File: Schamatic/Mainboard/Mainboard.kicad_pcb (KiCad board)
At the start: 2 copper layers, 85 parts, among them J1 BAT+, J10 BAT-, J2 M+1, J3 USART, J4 3.3V, J5 CONN_02X04, J6 FTSH-105-01-F-D-K, J7 M+2, J8 M-1, J9 M-2, Q1 BSC030P03NS3GAUMA1, SW1 B3U-1000P, SW2 B3U-1000P, SW3 B3U-1000P, SW4 B3U-1000P, U1 ACS781, U2 ADP2303ARDZ-3.3, U3 cc3220, U4 DEA202450BT, U5 MX25R3235F, U6 LSM9DS1, Y1 32.768kHz, Y2 40Mhz

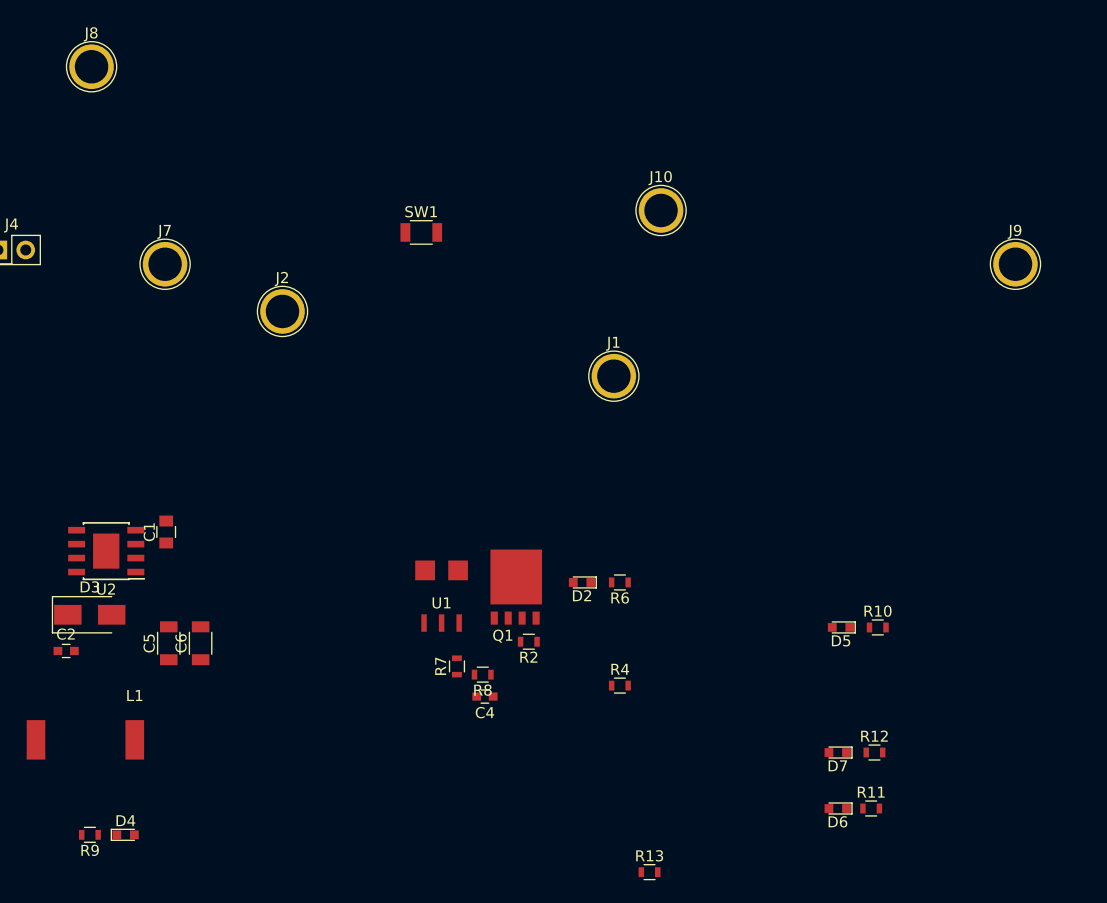
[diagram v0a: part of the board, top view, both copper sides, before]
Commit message: pushbutton switch
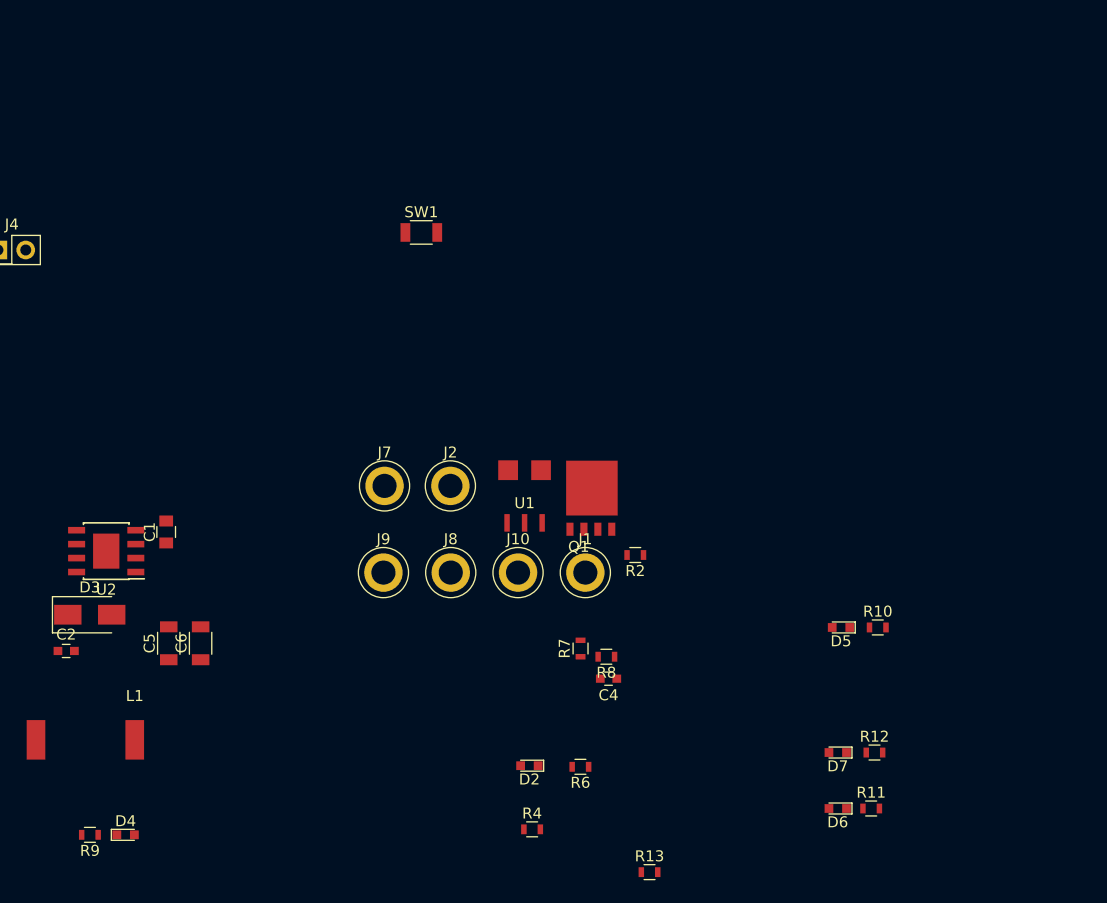
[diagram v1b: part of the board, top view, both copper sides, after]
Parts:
- moved J9 64.1 mm to (118.9, 50.4)
- moved J8 56.5 mm to (125.0, 50.4)
- moved J10 35.5 mm to (131.2, 50.4)
- moved J7 28.4 mm to (119.0, 42.5)
- moved J2 22.1 mm to (125.0, 42.5)
- moved J1 18.1 mm to (137.3, 50.4)
- moved D2 17.4 mm to (132.2, 68.0)
- moved R6 17.2 mm to (136.8, 68.1)
- moved R4 15.3 mm to (132.4, 73.8)
- moved R2 12.5 mm to (141.8, 48.8)
- moved U1 11.9 mm to (131.8, 43.5)
- moved R7 11.4 mm to (136.9, 57.3)
- moved R8 11.4 mm to (139.2, 58.1)
- moved C4 11.4 mm to (139.4, 60.1)
- moved Q1 10.6 mm to (135.9, 46.5)
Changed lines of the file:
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@@
     (mod_text_size 1 1)
     (mod_text_width 0.15)
-    (pad_size 1.524 1.524)
-    (pad_drill 0.762)
+    (pad_size 3.5 3.5)
+    (pad_drill 2.2)
     (pad_to_mask_clearance 0.2)
     (aux_axis_origin 0 0)
@@
   )
   (module Capacitors_SMD:C_0603 (layer F.Cu)
-    (at 128.15 61.7 180)
+    (at 139.41357 60.069586 180)
     (descr "Capacitor SMD 0603, reflow soldering, AVX (see smccp.pdf)")
     (tags "capacitor 0603")
@@
   )
   (module Dizzy:BSC030P (layer F.Cu)
-    (at 129 54.55)
+    (at 135.9 46.45)
     (fp_text reference Q1 (at 0.8 1.6) (layer F.SilkS)
       (effects (font (size 1 1) (thickness 0.15)))
@@
   )
   (module Resistors_SMD:R_0603 (layer F.Cu)
-    (at 132.15 56.7 180)
+    (at 141.85 48.8 180)
     (descr "Resistor SMD 0603, reflow soldering, Vishay (see dcrcw.pdf)")
     (tags "resistor 0603")
@@
   )
   (module Resistors_SMD:R_0603 (layer F.Cu)
-    (at 140.45 60.7)
+    (at 132.45 73.8)
     (descr "Resistor SMD 0603, reflow soldering, Vishay (see dcrcw.pdf)")
     (tags "resistor 0603")
@@
   )
   (module Resistors_SMD:R_0603 (layer F.Cu)
-    (at 140.45 51.3 180)
+    (at 136.85 68.1 180)
     (descr "Resistor SMD 0603, reflow soldering, Vishay (see dcrcw.pdf)")
     (tags "resistor 0603")
@@
   )
   (module Resistors_SMD:R_0603 (layer F.Cu)
-    (at 125.6 58.95 90)
+    (at 136.86357 57.319586 90)
     (descr "Resistor SMD 0603, reflow soldering, Vishay (see dcrcw.pdf)")
     (tags "resistor 0603")
@@
   )
   (module Resistors_SMD:R_0603 (layer F.Cu)
-    (at 127.95 59.7 180)
+    (at 139.21357 58.069586 180)
     (descr "Resistor SMD 0603, reflow soldering, Vishay (see dcrcw.pdf)")
     (tags "resistor 0603")
@@
   )
   (module Dizzy:ACS781 (layer F.Cu)
-    (at 124.2 52.6)
+    (at 131.76357 43.469586)
     (fp_text reference U1 (at 0 0.6) (layer F.SilkS)
       (effects (font (size 1 1) (thickness 0.15)))
@@
   )
   (module LEDs:LED_0603 (layer F.Cu)
-    (at 137 51.3 180)
+    (at 132.2 68 180)
     (descr "LED 0603 smd package")
     (tags "LED led 0603 SMD smd SMT smt smdled SMDLED smtled SMTLED")
@@
   )
   (module Connectors:1pin (layer F.Cu)
-    (at 139.9 32.5)
+    (at 137.299999 50.4)
     (descr "module 1 pin (ou trou mecanique de percage)")
     (tags DEV)
@@
     (fp_circle (center 0 0) (end 2.6 0) (layer F.CrtYd) (width 0.05))
     (fp_circle (center 0 0) (end 0 -2.286) (layer F.SilkS) (width 0.12))
-    (pad 1 thru_hole circle (at 0 0) (size 4.064 4.064) (drill 3.048) (layers *.Cu *.Mask)
+    (pad 1 thru_hole circle (at 0 0) (size 3.5 3.5) (drill 2.2) (layers *.Cu *.Mask)
       (net 79 "Net-(J1-Pad1)"))
   )
   (module Connectors:1pin (layer F.Cu)
-    (at 109.7 26.6)
+    (at 125 42.5)
     (descr "module 1 pin (ou trou mecanique de percage)")
     (tags DEV)
@@
     (fp_circle (center 0 0) (end 2.6 0) (layer F.CrtYd) (width 0.05))
     (fp_circle (center 0 0) (end 0 -2.286) (layer F.SilkS) (width 0.12))
-    (pad 1 thru_hole circle (at 0 0) (size 4.064 4.064) (drill 3.048) (layers *.Cu *.Mask)
+    (pad 1 thru_hole circle (at 0 0) (size 3.5 3.5) (drill 2.2) (layers *.Cu *.Mask)
       (net 78 "Net-(J2-Pad1)"))
   )
@@
   )
   (module Connectors:1pin (layer F.Cu)
-    (at 99 22.3)
+    (at 119 42.5)
     (descr "module 1 pin (ou trou mecanique de percage)")
     (tags DEV)
@@
     (fp_circle (center 0 0) (end 2.6 0) (layer F.CrtYd) (width 0.05))
     (fp_circle (center 0 0) (end 0 -2.286) (layer F.SilkS) (width 0.12))
-    (pad 1 thru_hole circle (at 0 0) (size 4.064 4.064) (drill 3.048) (layers *.Cu *.Mask)
+    (pad 1 thru_hole circle (at 0 0) (size 3.5 3.5) (drill 2.2) (layers *.Cu *.Mask)
       (net 78 "Net-(J2-Pad1)"))
   )
   (module Connectors:1pin (layer F.Cu)
-    (at 92.3 4.3)
+    (at 125.033333 50.4)
     (descr "module 1 pin (ou trou mecanique de percage)")
     (tags DEV)
@@
     (fp_circle (center 0 0) (end 2.6 0) (layer F.CrtYd) (width 0.05))
     (fp_circle (center 0 0) (end 0 -2.286) (layer F.SilkS) (width 0.12))
-    (pad 1 thru_hole circle (at 0 0) (size 4.064 4.064) (drill 3.048) (layers *.Cu *.Mask)
+    (pad 1 thru_hole circle (at 0 0) (size 3.5 3.5) (drill 2.2) (layers *.Cu *.Mask)
       (net 1 Earth))
   )
   (module Connectors:1pin (layer F.Cu)
-    (at 176.5 22.3)
+    (at 118.9 50.4)
     (descr "module 1 pin (ou trou mecanique de percage)")
     (tags DEV)
@@
     (fp_circle (center 0 0) (end 2.6 0) (layer F.CrtYd) (width 0.05))
     (fp_circle (center 0 0) (end 0 -2.286) (layer F.SilkS) (width 0.12))
-    (pad 1 thru_hole circle (at 0 0) (size 4.064 4.064) (drill 3.048) (layers *.Cu *.Mask)
+    (pad 1 thru_hole circle (at 0 0) (size 3.5 3.5) (drill 2.2) (layers *.Cu *.Mask)
       (net 1 Earth))
   )
   (module Connectors:1pin (layer F.Cu)
-    (at 144.2 17.4)
+    (at 131.166666 50.4)
     (descr "module 1 pin (ou trou mecanique de percage)")
     (tags DEV)
@@
     (fp_circle (center 0 0) (end 2.6 0) (layer F.CrtYd) (width 0.05))
     (fp_circle (center 0 0) (end 0 -2.286) (layer F.SilkS) (width 0.12))
-    (pad 1 thru_hole circle (at 0 0) (size 4.064 4.064) (drill 3.048) (layers *.Cu *.Mask)
-      (net 1 Earth))
-  )
+    (pad 1 thru_hole circle (at 0 0) (size 3.5 3.5) (drill 2.2) (layers *.Cu *.Mask)
+      (net 1 Earth))
+  )

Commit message: continue motherboard
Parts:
- added C35: 0.1uF, Capacitors_SMD:C_0603, F.Cu at (134.8, 44.6)
- added C36: 0.1uF, Capacitors_SMD:C_0603, F.Cu at (106.3, 104.8)
- added D1: D, Diodes_SMD:D_SMA, F.Cu at (147.2, 48.7)
- added D8: D, Diodes_SMD:D_SMA, F.Cu at (153.7, 48.7)
- added J11: PLUG+, Connectors:1pin, F.Cu at (147.0, 42.0)
- added J12: PLUG-, Connectors:1pin, F.Cu at (153.3, 56.5)
- added R17: 100k, Resistors_SMD:R_0603, F.Cu at (139.8, 46.7)
- added R18: 1.4M, Resistors_SMD:R_0603, F.Cu at (142.5, 42.4)
- added R19: 100k, Resistors_SMD:R_0603, F.Cu at (142.5, 45.1)
- added U7: LTC2954, Housings_DFN_QFN:DFN-8-1EP_2x3mm_Pitch0.5mm, F.Cu at (139.6, 42.8)
- added U8: LTC2876, Dizzy:LTC2876, F.Cu at (110.4, 104.7)
- R2: value R -> 100k
- moved SW4 111.6 mm to (108.0, 131.7), turned to 180 degrees
- moved R3 97.3 mm to (111.7, 41.8), turned to 90 degrees
- moved SW3 93.5 mm to (95.2, 97.9)
- moved D5 92.8 mm to (93.7, 119.7)
- moved R10 92.7 mm to (97.0, 119.5)
- moved J3 87.7 mm to (104.3, 98.8), turned to 270 degrees
- moved SW2 84.8 mm to (95.2, 102.4)
- moved C30 84.2 mm to (103.3, 120.1)
- moved D7 79.5 mm to (93.7, 110.3)
- moved R12 79.5 mm to (97.0, 110.3)
- moved D6 79.3 mm to (93.7, 115.0)
- moved R11 79.3 mm to (96.8, 115.0)
- moved R1 78.1 mm to (104.2, 122.5)
- moved J6 74.0 mm to (107.4, 121.3)
- moved R13 54.5 mm to (111.8, 122.3)
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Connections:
- J1 pad 1: Net-(J1-Pad1) -> Net-(D8-Pad2)
- J3 pad 1: RX -> RS-B
- J3 pad 2: TX -> RS-A
- Q1 pad 3: Net-(J1-Pad1) -> Net-(C35-Pad2)
- R2 pad 1: Net-(Q1-Pad2) -> Net-(R17-Pad1)
- R2 pad 2: Net-(J1-Pad1) -> Net-(C35-Pad2)
- SW1 pad 1: Net-(Q1-Pad2) -> Earth
- SW1 pad 2: Earth -> Net-(SW1-Pad2)
- U3 pad 3: Net-(U3-Pad3) -> DE

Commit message: working on mainboard PCB
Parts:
- added J13: MOUNT, Mounting_Holes:MountingHole_3.5mm_Pad, F.Cu at (145.8, 128.7)
- added J14: MOUNT, Mounting_Holes:MountingHole_3.5mm_Pad, F.Cu at (88.8, 128.8)
- added J15: MOUNT, Mounting_Holes:MountingHole_3.5mm_Pad, F.Cu at (146.0, 80.0)
- added J16: MOUNT, Mounting_Holes:MountingHole_3.5mm_Pad, F.Cu at (88.5, 80.0)
- added SW5: B3U-1000P, Resistors_SMD:R_1206, F.Cu at (88.8, 103.3)
- AE1: value AH316M245001-T -> ANT
- Q1: value BSC030P03NS3GAUMA1 -> p-MOSFET
- moved R15 83.2 mm to (97.8, 124.1), turned to 270 degrees
- moved R14 77.9 mm to (101.8, 130.9), turned to 180 degrees
- moved J1 61.3 mm to (139.5, 101.7), turned to 270 degrees
- moved J11 59.6 mm to (146.0, 101.6), turned to 270 degrees
- moved J4 51.2 mm to (89.0, 94.8), turned to 270 degrees
- moved D8 48.2 mm to (139.5, 94.8), turned to 270 degrees
- moved R16 47.2 mm to (100.4, 113.5), turned to 270 degrees
- moved D1 46.2 mm to (146.0, 94.9), turned to 270 degrees
- moved J2 41.8 mm to (116.5, 87.3)
- moved J7 41.8 mm to (110.5, 87.3)
- moved D3 41.8 mm to (88.9, 87.7), turned to 90 degrees
- moved R6 39.9 mm to (122.7, 81.1)
- moved Q1 38.6 mm to (133.4, 90.9)
- moved R17 38.6 mm to (131.8, 84.4)
- moved U1 38.6 mm to (123.3, 88.1)
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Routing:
- net 3v3: track 0.00 -> 186.8 mm, vias 0 -> 18
- net VDD_ANA: track 0.00 -> 50.6 mm
- net 12V: track 0.00 -> 47.1 mm
- net VDD_DIG: track 0.00 -> 42.9 mm
- net Net-(D5-Pad2): track 0.00 -> 40.1 mm, vias 0 -> 2
- net Net-(SW5-Pad2): track 0.00 -> 37.9 mm, vias 0 -> 2
- net Net-(C35-Pad2): track 0.00 -> 34.9 mm, vias 0 -> 2
- net SCL: track 0.00 -> 34.0 mm, vias 0 -> 3
- net Net-(SW3-Pad2): track 0.00 -> 32.1 mm, vias 0 -> 2
- net Net-(D6-Pad2): track 0.00 -> 31.9 mm, vias 0 -> 2
- net SDA: track 0.00 -> 31.0 mm, vias 0 -> 2
- net nRESET: track 0.00 -> 30.2 mm, vias 0 -> 2
- net Earth: track 0.00 -> 29.7 mm, vias 0 -> 59
- net Net-(SW2-Pad2): track 0.00 -> 29.0 mm, vias 0 -> 2
- net Net-(D7-Pad2): track 0.00 -> 25.2 mm, vias 0 -> 2
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- added copper zone on F.Cu, net 12V
- added copper zone on In2.Cu, net 3v3
- added copper zone on B.Cu, net Earth
- added copper zone on F.Cu, net Earth
- added copper zone on In1.Cu, net Earth
- added copper zone on F.Cu, net Net-(C35-Pad2)
- added copper zone on F.Cu, net Net-(D1-Pad2)
- added copper zone on F.Cu, net Net-(D8-Pad2)
- added copper zone on F.Cu, net Net-(J2-Pad1)
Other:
- board outline added: 70 x 74.3 mm
- copper layers 2 -> 4
- net class Default: clearance 0.2 -> 0.13; trace_width 0.25 -> 0.13; via_dia 0.6 -> 0.4; via_drill 0.4 -> 0.25
- rule trace_clearance: 0.2 -> 0.13
- rule trace_min: 0.2 -> 0.1
- rule via_min_drill: 0.3 -> 0.2
- rule via_min_size: 0.4 -> 0.2
- board text added: "DizzyRobot"

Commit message: mainboard pcb more or less complete
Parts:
- added REF**: VIA-0.4, Dizzy:VIA-0.4, F.Cu at (105.8, 104.6)
- added REF**: VIA-0.4, Dizzy:VIA-0.4, F.Cu at (101.0, 117.6)
- added REF**: VIA-0.4, Dizzy:VIA-0.4, F.Cu at (125.4, 114.0)
- added REF**: VIA-0.4, Dizzy:VIA-0.4, F.Cu at (125.4, 114.8)
- added REF**: VIA-0.4, Dizzy:VIA-0.4, F.Cu at (125.4, 113.2)
- added REF**: VIA-0.4, Dizzy:VIA-0.4, F.Cu at (125.4, 107.6)
- added REF**: VIA-0.4, Dizzy:VIA-0.4, F.Cu at (125.4, 110.0)
- added REF**: VIA-0.4, Dizzy:VIA-0.4, F.Cu at (125.4, 108.4)
- added REF**: VIA-0.4, Dizzy:VIA-0.4, F.Cu at (125.4, 110.8)
- added REF**: VIA-0.4, Dizzy:VIA-0.4, F.Cu at (125.4, 109.2)
- added REF**: VIA-0.4, Dizzy:VIA-0.4, F.Cu at (124.6, 111.6)
- added REF**: VIA-0.4, Dizzy:VIA-0.4, F.Cu at (124.6, 112.4)
- added REF**: VIA-0.4, Dizzy:VIA-0.4, F.Cu at (92.3, 116.8)
- added REF**: VIA-0.4, Dizzy:VIA-0.4, F.Cu at (124.6, 114.0)
- added REF**: VIA-0.4, Dizzy:VIA-0.4, F.Cu at (124.6, 114.8)
- added REF**: VIA-0.4, Dizzy:VIA-0.4, F.Cu at (124.6, 113.2)
- added REF**: VIA-0.4, Dizzy:VIA-0.4, F.Cu at (124.6, 107.6)
- added REF**: VIA-0.4, Dizzy:VIA-0.4, F.Cu at (124.6, 110.0)
- added REF**: VIA-0.4, Dizzy:VIA-0.4, F.Cu at (124.6, 108.4)
- added REF**: VIA-0.4, Dizzy:VIA-0.4, F.Cu at (124.6, 110.8)
- added REF**: VIA-0.4, Dizzy:VIA-0.4, F.Cu at (124.6, 109.2)
- added REF**: VIA-0.4, Dizzy:VIA-0.4, F.Cu at (123.8, 111.6)
- added REF**: VIA-0.4, Dizzy:VIA-0.4, F.Cu at (123.8, 112.4)
- added REF**: VIA-0.4, Dizzy:VIA-0.4, F.Cu at (95.5, 123.2)
- added REF**: VIA-0.4, Dizzy:VIA-0.4, F.Cu at (123.8, 114.0)
- added REF**: VIA-0.4, Dizzy:VIA-0.4, F.Cu at (123.8, 114.8)
- added REF**: VIA-0.4, Dizzy:VIA-0.4, F.Cu at (123.8, 113.2)
- added REF**: VIA-0.4, Dizzy:VIA-0.4, F.Cu at (123.8, 107.6)
- added REF**: VIA-0.4, Dizzy:VIA-0.4, F.Cu at (123.8, 110.0)
- added REF**: VIA-0.4, Dizzy:VIA-0.4, F.Cu at (123.8, 108.4)
- added REF**: VIA-0.4, Dizzy:VIA-0.4, F.Cu at (123.8, 110.8)
- added REF**: VIA-0.4, Dizzy:VIA-0.4, F.Cu at (123.8, 109.2)
- added REF**: VIA-0.4, Dizzy:VIA-0.4, F.Cu at (123.0, 111.6)
- added REF**: VIA-0.4, Dizzy:VIA-0.4, F.Cu at (123.0, 112.4)
- added REF**: VIA-0.4, Dizzy:VIA-0.4, F.Cu at (118.8, 129.0)
- added REF**: VIA-0.4, Dizzy:VIA-0.4, F.Cu at (123.0, 114.0)
- added REF**: VIA-0.4, Dizzy:VIA-0.4, F.Cu at (123.0, 114.8)
- added REF**: VIA-0.4, Dizzy:VIA-0.4, F.Cu at (123.0, 113.2)
- added REF**: VIA-0.4, Dizzy:VIA-0.4, F.Cu at (123.0, 107.6)
- added REF**: VIA-0.4, Dizzy:VIA-0.4, F.Cu at (123.0, 110.0)
- added REF**: VIA-0.4, Dizzy:VIA-0.4, F.Cu at (123.0, 108.4)
- added REF**: VIA-0.4, Dizzy:VIA-0.4, F.Cu at (123.0, 110.8)
- added REF**: VIA-0.4, Dizzy:VIA-0.4, F.Cu at (123.0, 109.2)
- added REF**: VIA-0.4, Dizzy:VIA-0.4, F.Cu at (122.2, 111.6)
- added REF**: VIA-0.4, Dizzy:VIA-0.4, F.Cu at (122.2, 112.4)
- added REF**: VIA-0.4, Dizzy:VIA-0.4, F.Cu at (110.7, 129.0)
- added REF**: VIA-0.4, Dizzy:VIA-0.4, F.Cu at (122.2, 114.0)
- added REF**: VIA-0.4, Dizzy:VIA-0.4, F.Cu at (122.2, 114.8)
- added REF**: VIA-0.4, Dizzy:VIA-0.4, F.Cu at (122.2, 113.2)
- added REF**: VIA-0.4, Dizzy:VIA-0.4, F.Cu at (122.2, 107.6)
- added REF**: VIA-0.4, Dizzy:VIA-0.4, F.Cu at (122.2, 110.0)
- added REF**: VIA-0.4, Dizzy:VIA-0.4, F.Cu at (122.2, 108.4)
- added REF**: VIA-0.4, Dizzy:VIA-0.4, F.Cu at (122.2, 110.8)
- added REF**: VIA-0.4, Dizzy:VIA-0.4, F.Cu at (122.2, 109.2)
- added REF**: VIA-0.4, Dizzy:VIA-0.4, F.Cu at (121.4, 111.6)
- added REF**: VIA-0.4, Dizzy:VIA-0.4, F.Cu at (121.4, 112.4)
- added REF**: VIA-0.4, Dizzy:VIA-0.4, F.Cu at (114.1, 124.0)
- added REF**: VIA-0.4, Dizzy:VIA-0.4, F.Cu at (121.4, 114.0)
- added REF**: VIA-0.4, Dizzy:VIA-0.4, F.Cu at (121.4, 114.8)
- added REF**: VIA-0.4, Dizzy:VIA-0.4, F.Cu at (121.4, 113.2)
- added REF**: VIA-0.4, Dizzy:VIA-0.4, F.Cu at (121.4, 107.6)
- added REF**: VIA-0.4, Dizzy:VIA-0.4, F.Cu at (121.4, 110.0)
- added REF**: VIA-0.4, Dizzy:VIA-0.4, F.Cu at (121.4, 108.4)
- added REF**: VIA-0.4, Dizzy:VIA-0.4, F.Cu at (121.4, 110.8)
- added REF**: VIA-0.4, Dizzy:VIA-0.4, F.Cu at (121.4, 109.2)
- added REF**: VIA-0.4, Dizzy:VIA-0.4, F.Cu at (120.6, 111.6)
- added REF**: VIA-0.4, Dizzy:VIA-0.4, F.Cu at (120.6, 112.4)
- added REF**: VIA-0.4, Dizzy:VIA-0.4, F.Cu at (130.0, 126.2)
- added REF**: VIA-0.4, Dizzy:VIA-0.4, F.Cu at (120.6, 114.0)
- added REF**: VIA-0.4, Dizzy:VIA-0.4, F.Cu at (120.6, 114.8)
- added REF**: VIA-0.4, Dizzy:VIA-0.4, F.Cu at (120.6, 113.2)
- added REF**: VIA-0.4, Dizzy:VIA-0.4, F.Cu at (120.6, 107.6)
- added REF**: VIA-0.4, Dizzy:VIA-0.4, F.Cu at (120.6, 110.0)
- added REF**: VIA-0.4, Dizzy:VIA-0.4, F.Cu at (120.6, 108.4)
- added REF**: VIA-0.4, Dizzy:VIA-0.4, F.Cu at (120.6, 110.8)
- added REF**: VIA-0.4, Dizzy:VIA-0.4, F.Cu at (120.6, 109.2)
- added REF**: VIA-0.4, Dizzy:VIA-0.4, F.Cu at (119.8, 111.6)
- added REF**: VIA-0.4, Dizzy:VIA-0.4, F.Cu at (119.8, 112.4)
- added REF**: VIA-0.4, Dizzy:VIA-0.4, F.Cu at (129.3, 126.0)
- added REF**: VIA-0.4, Dizzy:VIA-0.4, F.Cu at (119.8, 114.0)
- added REF**: VIA-0.4, Dizzy:VIA-0.4, F.Cu at (119.8, 114.8)
- added REF**: VIA-0.4, Dizzy:VIA-0.4, F.Cu at (119.8, 113.2)
- added REF**: VIA-0.4, Dizzy:VIA-0.4, F.Cu at (119.8, 107.6)
- added REF**: VIA-0.4, Dizzy:VIA-0.4, F.Cu at (119.8, 110.0)
- added REF**: VIA-0.4, Dizzy:VIA-0.4, F.Cu at (119.8, 108.4)
- added REF**: VIA-0.4, Dizzy:VIA-0.4, F.Cu at (119.8, 110.8)
- added REF**: VIA-0.4, Dizzy:VIA-0.4, F.Cu at (119.8, 109.2)
- added REF**: VIA-0.4, Dizzy:VIA-0.4, F.Cu at (119.0, 114.8)
- added REF**: VIA-0.4, Dizzy:VIA-0.4, F.Cu at (119.0, 107.6)
- added REF**: VIA-0.4, Dizzy:VIA-0.4, F.Cu at (131.4, 127.2)
- added REF**: VIA-0.4, Dizzy:VIA-0.4, F.Cu at (119.0, 108.4)
- added REF**: VIA-0.4, Dizzy:VIA-0.4, F.Cu at (119.0, 109.2)
- added REF**: VIA-0.4, Dizzy:VIA-0.4, F.Cu at (119.0, 110.0)
- added REF**: VIA-0.4, Dizzy:VIA-0.4, F.Cu at (119.0, 110.8)
- added REF**: VIA-0.4, Dizzy:VIA-0.4, F.Cu at (119.0, 111.6)
- added REF**: VIA-0.4, Dizzy:VIA-0.4, F.Cu at (119.0, 112.4)
- added REF**: VIA-0.4, Dizzy:VIA-0.4, F.Cu at (119.0, 113.2)
- added REF**: VIA-0.4, Dizzy:VIA-0.4, F.Cu at (119.0, 114.0)
- added REF**: VIA-0.4, Dizzy:VIA-0.4, F.Cu at (129.4, 126.8)
- added REF**: VIA-0.4, Dizzy:VIA-0.4, F.Cu at (103.3, 112.2)
- added REF**: VIA-0.4, Dizzy:VIA-0.4, F.Cu at (128.5, 126.8)
- added REF**: VIA-0.4, Dizzy:VIA-0.4, F.Cu at (128.6, 125.2)
- added REF**: VIA-0.4, Dizzy:VIA-0.4, F.Cu at (128.6, 124.4)
- added REF**: VIA-0.4, Dizzy:VIA-0.4, F.Cu at (128.6, 126.0)
- added REF**: VIA-0.4, Dizzy:VIA-0.4, F.Cu at (128.6, 123.6)
- added REF**: VIA-0.4, Dizzy:VIA-0.4, F.Cu at (123.4, 129.0)
- added REF**: VIA-0.4, Dizzy:VIA-0.4, F.Cu at (123.4, 129.8)
- added REF**: VIA-0.4, Dizzy:VIA-0.4, F.Cu at (123.4, 131.4)
- added REF**: VIA-0.4, Dizzy:VIA-0.4, F.Cu at (123.4, 130.6)
- added REF**: VIA-0.4, Dizzy:VIA-0.4, F.Cu at (123.4, 127.4)
- added REF**: VIA-0.4, Dizzy:VIA-0.4, F.Cu at (106.4, 113.4)
- added REF**: VIA-0.4, Dizzy:VIA-0.4, F.Cu at (123.4, 128.2)
- added REF**: VIA-0.4, Dizzy:VIA-0.4, F.Cu at (124.0, 123.4)
- added REF**: VIA-0.4, Dizzy:VIA-0.4, F.Cu at (124.0, 120.2)
- added REF**: VIA-0.4, Dizzy:VIA-0.4, F.Cu at (124.0, 119.4)
- added REF**: VIA-0.4, Dizzy:VIA-0.4, F.Cu at (124.0, 121.0)
- added REF**: VIA-0.4, Dizzy:VIA-0.4, F.Cu at (124.0, 122.6)
- added REF**: VIA-0.4, Dizzy:VIA-0.4, F.Cu at (124.0, 121.8)
- added REF**: VIA-0.4, Dizzy:VIA-0.4, F.Cu at (127.8, 118.0)
- added REF**: VIA-0.4, Dizzy:VIA-0.4, F.Cu at (127.8, 118.8)
- added REF**: VIA-0.4, Dizzy:VIA-0.4, F.Cu at (127.8, 119.6)
- added REF**: VIA-0.4, Dizzy:VIA-0.4, F.Cu at (94.7, 105.8)
- added REF**: VIA-0.4, Dizzy:VIA-0.4, F.Cu at (127.8, 121.2)
- added REF**: VIA-0.4, Dizzy:VIA-0.4, F.Cu at (127.8, 120.4)
- added REF**: VIA-0.4, Dizzy:VIA-0.4, F.Cu at (127.8, 122.0)
- added REF**: VIA-0.4, Dizzy:VIA-0.4, F.Cu at (127.8, 125.2)
- added REF**: VIA-0.4, Dizzy:VIA-0.4, F.Cu at (127.8, 123.6)
- added REF**: VIA-0.4, Dizzy:VIA-0.4, F.Cu at (127.8, 122.8)
- added REF**: VIA-0.4, Dizzy:VIA-0.4, F.Cu at (127.8, 124.4)
- added REF**: VIA-0.4, Dizzy:VIA-0.4, F.Cu at (124.6, 118.6)
- added REF**: VIA-0.4, Dizzy:VIA-0.4, F.Cu at (130.6, 126.8)
- added REF**: VIA-0.4, Dizzy:VIA-0.4, F.Cu at (130.6, 127.6)
- added REF**: VIA-0.4, Dizzy:VIA-0.4, F.Cu at (103.7, 94.6)
- added REF**: VIA-0.4, Dizzy:VIA-0.4, F.Cu at (130.6, 129.2)
- added REF**: VIA-0.4, Dizzy:VIA-0.4, F.Cu at (130.6, 130.0)
- added REF**: VIA-0.4, Dizzy:VIA-0.4, F.Cu at (130.6, 128.4)
- added REF**: VIA-0.4, Dizzy:VIA-0.4, F.Cu at (131.4, 128.0)
- added REF**: VIA-0.4, Dizzy:VIA-0.4, F.Cu at (131.4, 130.4)
- added REF**: VIA-0.4, Dizzy:VIA-0.4, F.Cu at (131.4, 128.8)
- added REF**: VIA-0.4, Dizzy:VIA-0.4, F.Cu at (131.4, 131.2)
- added REF**: VIA-0.4, Dizzy:VIA-0.4, F.Cu at (131.4, 129.6)
- added REF**: VIA-0.4, Dizzy:VIA-0.4, F.Cu at (124.0, 128.2)
- added REF**: VIA-0.4, Dizzy:VIA-0.4, F.Cu at (124.0, 129.0)
- added REF**: VIA-0.4, Dizzy:VIA-0.4, F.Cu at (108.8, 93.0)
- added REF**: VIA-0.4, Dizzy:VIA-0.4, F.Cu at (124.0, 130.6)
- added REF**: VIA-0.4, Dizzy:VIA-0.4, F.Cu at (124.0, 131.4)
- added REF**: VIA-0.4, Dizzy:VIA-0.4, F.Cu at (124.0, 129.8)
- added REF**: VIA-0.4, Dizzy:VIA-0.4, F.Cu at (124.0, 124.2)
- added REF**: VIA-0.4, Dizzy:VIA-0.4, F.Cu at (124.0, 126.6)
- added REF**: VIA-0.4, Dizzy:VIA-0.4, F.Cu at (124.0, 125.0)
- added REF**: VIA-0.4, Dizzy:VIA-0.4, F.Cu at (124.0, 127.4)
- added REF**: VIA-0.4, Dizzy:VIA-0.4, F.Cu at (124.0, 125.8)
- added REF**: VIA-0.4, Dizzy:VIA-0.4, F.Cu at (127.0, 122.0)
- added REF**: VIA-0.4, Dizzy:VIA-0.4, F.Cu at (127.0, 122.8)
- added REF**: VIA-0.4, Dizzy:VIA-0.4, F.Cu at (99.6, 93.6)
- added REF**: VIA-0.4, Dizzy:VIA-0.4, F.Cu at (127.0, 124.4)
- added REF**: VIA-0.4, Dizzy:VIA-0.4, F.Cu at (127.0, 125.2)
- added REF**: VIA-0.4, Dizzy:VIA-0.4, F.Cu at (127.0, 123.6)
- added REF**: VIA-0.4, Dizzy:VIA-0.4, F.Cu at (127.0, 118.0)
- added REF**: VIA-0.4, Dizzy:VIA-0.4, F.Cu at (127.0, 120.4)
- added REF**: VIA-0.4, Dizzy:VIA-0.4, F.Cu at (127.0, 118.8)
- added REF**: VIA-0.4, Dizzy:VIA-0.4, F.Cu at (127.0, 121.2)
- added REF**: VIA-0.4, Dizzy:VIA-0.4, F.Cu at (127.0, 119.6)
- added REF**: VIA-0.4, Dizzy:VIA-0.4, F.Cu at (124.6, 123.4)
- added REF**: VIA-0.4, Dizzy:VIA-0.4, F.Cu at (124.6, 124.2)
- added REF**: VIA-0.4, Dizzy:VIA-0.4, F.Cu at (99.7, 96.4)
- added REF**: VIA-0.4, Dizzy:VIA-0.4, F.Cu at (124.6, 125.8)
- added REF**: VIA-0.4, Dizzy:VIA-0.4, F.Cu at (124.6, 126.6)
- added REF**: VIA-0.4, Dizzy:VIA-0.4, F.Cu at (124.6, 125.0)
- added REF**: VIA-0.4, Dizzy:VIA-0.4, F.Cu at (124.6, 119.4)
- added REF**: VIA-0.4, Dizzy:VIA-0.4, F.Cu at (124.6, 121.8)
- added REF**: VIA-0.4, Dizzy:VIA-0.4, F.Cu at (124.6, 120.2)
- added REF**: VIA-0.4, Dizzy:VIA-0.4, F.Cu at (124.6, 122.6)
- added REF**: VIA-0.4, Dizzy:VIA-0.4, F.Cu at (124.6, 121.0)
- added REF**: VIA-0.4, Dizzy:VIA-0.4, F.Cu at (126.2, 111.6)
- added REF**: VIA-0.4, Dizzy:VIA-0.4, F.Cu at (126.2, 112.4)
- added REF**: VIA-0.4, Dizzy:VIA-0.4, F.Cu at (99.7, 101.2)
- added REF**: VIA-0.4, Dizzy:VIA-0.4, F.Cu at (126.2, 114.0)
- added REF**: VIA-0.4, Dizzy:VIA-0.4, F.Cu at (126.2, 114.8)
- added REF**: VIA-0.4, Dizzy:VIA-0.4, F.Cu at (126.2, 113.2)
- added REF**: VIA-0.4, Dizzy:VIA-0.4, F.Cu at (126.2, 107.6)
- added REF**: VIA-0.4, Dizzy:VIA-0.4, F.Cu at (126.2, 110.0)
- added REF**: VIA-0.4, Dizzy:VIA-0.4, F.Cu at (126.2, 108.4)
- added REF**: VIA-0.4, Dizzy:VIA-0.4, F.Cu at (126.2, 110.8)
- added REF**: VIA-0.4, Dizzy:VIA-0.4, F.Cu at (126.2, 109.2)
- added REF**: VIA-0.4, Dizzy:VIA-0.4, F.Cu at (125.4, 111.6)
- added REF**: VIA-0.4, Dizzy:VIA-0.4, F.Cu at (125.4, 112.4)
- J8: footprint Connectors:1pin -> 1pin
- moved R9 8.02 mm to (100.8, 90.5), turned to 0 degrees
- moved D4 6.91 mm to (98.2, 90.5), turned to 180 degrees
- moved R14 6.21 mm to (107.8, 129.3), turned to 0 degrees
- moved C32 5.01 mm to (100.7, 129.2), turned to 270 degrees
- moved C2 4.50 mm to (99.2, 87.3)
- moved C5 4.50 mm to (104.2, 87.5)
- moved C6 4.50 mm to (104.2, 90.5)
- moved D3 4.50 mm to (93.0, 89.5)
- moved U2 4.50 mm to (102.2, 82.4)
- moved J16 4.20 mm to (92.7, 80.1)
- moved J14 3.90 mm to (92.7, 128.7)
- moved SW3 3.74 mm to (92.1, 121.0)
- moved D7 3.66 mm to (97.3, 110.8)
- moved D6 3.65 mm to (97.3, 115.4)
- moved U6 3.64 mm to (101.5, 125.1), turned to 180 degrees
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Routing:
- net 3v3: track 186.8 -> 138.1 mm, vias 18 -> 16
- net Net-(SW3-Pad2): track 32.1 -> 27.3 mm
- net Net-(SW5-Pad2): track 37.9 -> 34.4 mm
- net Net-(C2-Pad1): track 23.0 -> 19.6 mm
- net Net-(D5-Pad2): track 40.1 -> 36.8 mm
- net Net-(SW2-Pad2): track 29.0 -> 25.8 mm
- net SCL: track 34.0 -> 30.9 mm
- net Net-(D7-Pad2): track 25.2 -> 22.2 mm
- net Net-(R3-Pad2): track 6.08 -> 3.06 mm
- net Net-(D6-Pad2): track 31.9 -> 29.0 mm
- net nRESET: track 30.2 -> 27.6 mm
- net 12V: track 47.1 -> 49.1 mm
- net SDA: track 31.0 -> 29.2 mm
- net Net-(C34-Pad1): track 1.93 -> 3.37 mm
- net Net-(C32-Pad1): track 2.00 -> 3.08 mm
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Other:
- board size 70 x 74.3 mm -> 70 x 74.5 mm

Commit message: motherboard minor changes
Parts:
- C3, C4: value 0.01uF -> 0.1uF 25V
- J6: value FTSH-105-01-F-D-K -> JTAG
- J8: footprint 1pin -> Connectors:1pin
- R18: value 1.4M -> 140K
- R19: value 100k -> 10k
- R4: value R -> 200K 1%
- R5: value R -> 10K 1%
- R7: value R -> 22k 1%
- R8: value R -> 10k 1%
- U4: value DEA202450BT -> DEA202450BT-3201B2; footprint Dizzy:DEA202450BT -> Dizzy:DEA202450BT-3201B2
- moved REF** 1.00 mm to (124.6, 121.2)
- moved U4 0.92 mm to (125.7, 121.0)
- moved REF** 0.52 mm to (124.8, 120.5)
- moved REF** 0.30 mm to (126.7, 120.5)
- moved REF** 0.22 mm to (124.6, 119.6)
- moved REF** 0.20 mm to (124.6, 118.8)
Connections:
- U4 pad 1: Net-(U3-Pad31) -> Earth
- U4 pad 2: Earth -> Net-(U3-Pad31)
- U4 pad 3: Net-(L6-Pad1) -> Earth
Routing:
- net Earth: track 30.7 -> 31.3 mm
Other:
- board size 70 x 74.5 mm -> 60.3 x 55.7 mm
